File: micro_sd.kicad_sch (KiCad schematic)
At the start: 8 parts, among them IC2 CM1624-08DE, J1 47352-1001, U1 SIP32402ADNP-T1GE4

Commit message: Added footprint for components in Schematics. Updated LED resistors
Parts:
- C33, C34: footprint (none) -> Capacitor_SMD:C_0805_2012Metric
- C35, C36: footprint (none) -> Capacitor_SMD:C_0201_0603Metric
- R8: footprint (none) -> Resistor_SMD:R_0805_2012Metric
- U1: footprint Vishay-T16-0143-04_2016-C-* -> Personal:Vishay-T16-0143-04_2016-C-MFG
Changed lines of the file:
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@@
       (effects (font (size 1.27 1.27)) (justify left))
     )
-    (property "Footprint" "" (id 2) (at 26.67 33.02 0)
+    (property "Footprint" "Capacitor_SMD:C_0805_2012Metric" (id 2) (at 26.67 33.02 0)
       (effects (font (size 1.27 1.27)) hide)
     )
@@
       (effects (font (size 1.27 1.27)) (justify left))
     )
-    (property "Footprint" "" (id 2) (at 172.72 56.515 0)
+    (property "Footprint" "Capacitor_SMD:C_0201_0603Metric" (id 2) (at 172.72 56.515 0)
       (effects (font (size 1.27 1.27)) hide)
     )
@@
       (effects (font (size 1.27 1.27)) (justify left))
     )
-    (property "Footprint" "" (id 2) (at 162.56 56.515 0)
+    (property "Footprint" "Capacitor_SMD:C_0201_0603Metric" (id 2) (at 162.56 56.515 0)
       (effects (font (size 1.27 1.27)) hide)
     )
@@
       (effects (font (size 1.27 1.27)) (justify left))
     )
-    (property "Footprint" "" (id 2) (at 40.64 33.02 0)
+    (property "Footprint" "Resistor_SMD:R_0805_2012Metric" (id 2) (at 40.64 33.02 0)
       (effects (font (size 1.27 1.27)) hide)
     )
@@
       (effects (font (size 1.27 1.27)) (justify left))
     )
-    (property "Footprint" "" (id 2) (at 90.17 30.48 0)
+    (property "Footprint" "Capacitor_SMD:C_0805_2012Metric" (id 2) (at 90.17 30.48 0)
       (effects (font (size 1.27 1.27)) hide)
     )
@@
     (property "Reference" "U1" (id 0) (at 59.69 15.24 0))
     (property "Value" "SIP32402ADNP-T1GE4" (id 1) (at 59.69 17.78 0))
-    (property "Footprint" "Vishay-T16-0143-04_2016-C-*" (id 2) (at 44.45 12.7 0)
-      (effects (font (size 1.27 1.27)) (justify left) hide)
-    )
+    (property "Footprint" "Personal:Vishay-T16-0143-04_2016-C-MFG" (id 2) (at 44.45 12.7 0)
+      (effects (font (size 1.27 1.27)) (justify left) hide)
+    )

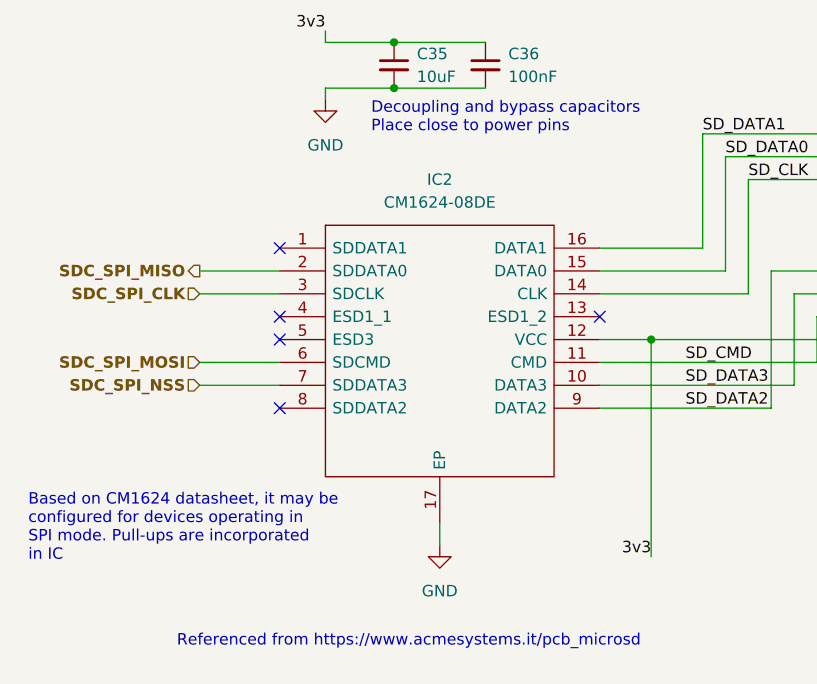
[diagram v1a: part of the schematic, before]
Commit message: Added preliminary PCL layout
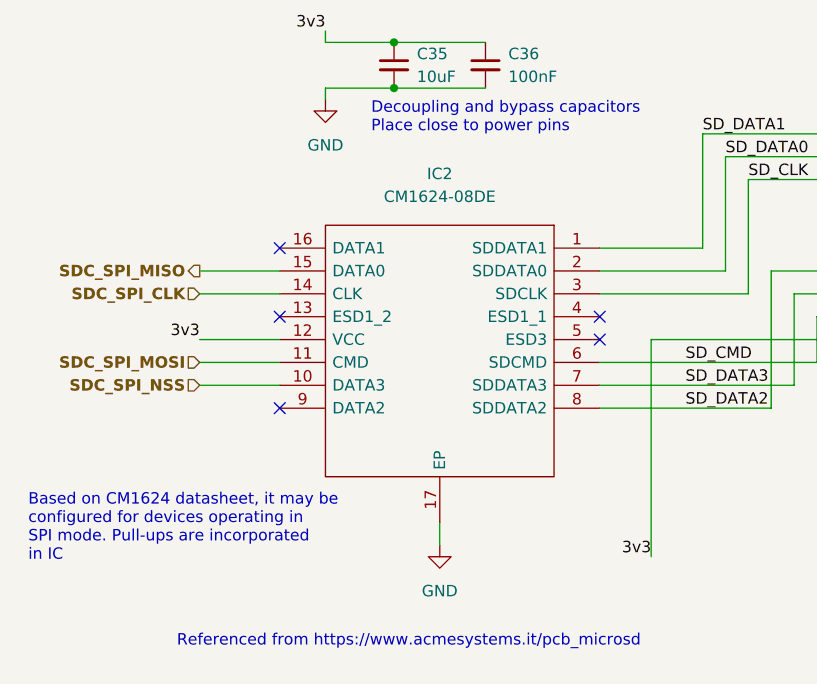
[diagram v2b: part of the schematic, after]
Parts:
- C35, C36: footprint Capacitor_SMD:C_0201_0603Metric -> Capacitor_SMD:C_0603_1608Metric
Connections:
- net SDC_SPI_CLK: now also IC2.14 (CLK); no longer IC2.3 (SDCLK)
- net SDC_SPI_MISO: now also IC2.15 (DATA0); no longer IC2.2 (SDDATA0)
- net SDC_SPI_MOSI: now also IC2.11 (CMD); no longer IC2.6 (SDCMD)
- net SDC_SPI_NSS: now also IC2.10 (DATA3); no longer IC2.7 (SDDATA3)
- net SD_CLK: now also IC2.3 (SDCLK); no longer IC2.14 (CLK)
- net SD_CMD: now also IC2.6 (SDCMD); no longer IC2.11 (CMD)
- net SD_DATA0: now also IC2.2 (SDDATA0); no longer IC2.15 (DATA0)
- net SD_DATA1: now also IC2.1 (SDDATA1); no longer IC2.16 (DATA1)
- net SD_DATA2: now also IC2.8 (SDDATA2); no longer IC2.9 (DATA2)
- net SD_DATA3: now also IC2.7 (SDDATA3); no longer IC2.10 (DATA3)
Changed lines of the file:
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@@
   (junction (at 162.56 59.055) (diameter 0) (color 0 0 0 0)
-  )
-  (junction (at 191.135 86.995) (diameter 0) (color 0 0 0 0)
   )
   (junction (at 40.64 27.94) (diameter 0) (color 0 0 0 0)
@@
   (no_connect (at 149.86 76.835))
   (no_connect (at 149.86 84.455))
-  (no_connect (at 149.86 86.995))
+  (no_connect (at 185.42 86.995))
   (wire (pts (xy 246.38 86.995) (xy 251.46 86.995))
     (stroke (width 0) (type default) (color 0 0 0 0))
@@
     (stroke (width 0) (type default) (color 0 0 0 0))
   )
+  (wire (pts (xy 140.97 86.995) (xy 149.86 86.995))
+    (stroke (width 0) (type default) (color 0 0 0 0))
+  )
   (wire (pts (xy 140.97 81.915) (xy 149.86 81.915))
     (stroke (width 0) (type default) (color 0 0 0 0))
@@
   )
   (wire (pts (xy 72.39 22.86) (xy 90.17 22.86))
-    (stroke (width 0) (type default) (color 0 0 0 0))
-  )
-  (wire (pts (xy 185.42 86.995) (xy 191.135 86.995))
     (stroke (width 0) (type default) (color 0 0 0 0))
   )
@@
     (effects (font (size 1.27 1.27)) (justify left bottom))
   )
+  (label "3v3" (at 140.97 86.995 180)
+    (effects (font (size 1.27 1.27)) (justify right bottom))
+  )
   (label "3v3" (at 191.135 111.125 180)
     (effects (font (size 1.27 1.27)) (justify right bottom))
@@
       (effects (font (size 1.27 1.27)) (justify left))
     )
-    (property "Footprint" "Capacitor_SMD:C_0201_0603Metric" (id 2) (at 172.72 56.515 0)
+    (property "Footprint" "Capacitor_SMD:C_0603_1608Metric" (id 2) (at 172.72 56.515 0)
       (effects (font (size 1.27 1.27)) hide)
     )
@@
       (effects (font (size 1.27 1.27)) (justify left))
     )
-    (property "Footprint" "Capacitor_SMD:C_0201_0603Metric" (id 2) (at 162.56 56.515 0)
+    (property "Footprint" "Capacitor_SMD:C_0603_1608Metric" (id 2) (at 162.56 56.515 0)
       (effects (font (size 1.27 1.27)) hide)
     )
@@
     (pin "8")
   )
-  (symbol (lib_id "SamacSys_Parts:CM1624-08DE") (at 149.86 76.835 0) (unit 1)
-    (in_bom yes) (on_board yes) (fields_autoplaced)
-    (property "Reference" "IC2" (id 0) (at 167.64 69.215 0))
-    (property "Value" "CM1624-08DE" (id 1) (at 167.64 71.755 0))
-    (property "Footprint" "SamacSys_Parts:SON40P135X330X55-17N" (id 2) (at 181.61 74.295 0)
-      (effects (font (size 1.27 1.27)) (justify left) hide)
-    )
-    (property "Datasheet" "http://www.onsemi.com/pub/Collateral/CM1624-D.PDF" (id 3) (at 181.61 76.835 0)
-      (effects (font (size 1.27 1.27)) (justify left) hide)
-    )
-    (property "Description" "ON SEMICONDUCTOR - CM1624-08DE. - EMI Filter, 4-Channel, ESD Protection, 300MHz, Line Protection, UDFN-16" (id 4) (at 181.61 79.375 0)
-      (effects (font (size 1.27 1.27)) (justify left) hide)
-    )
-    (property "Height" "0.55" (id 5) (at 181.61 81.915 0)
-      (effects (font (size 1.27 1.27)) (justify left) hide)
-    )
-    (property "Manufacturer_Name" "onsemi" (id 6) (at 181.61 84.455 0)
-      (effects (font (size 1.27 1.27)) (justify left) hide)
-    )
-    (property "Manufacturer_Part_Number" "CM1624-08DE" (id 7) (at 181.61 86.995 0)
-      (effects (font (size 1.27 1.27)) (justify left) hide)
-    )
-    (property "Mouser Part Number" "748-CM1624-08DE" (id 8) (at 181.61 89.535 0)
-      (effects (font (size 1.27 1.27)) (justify left) hide)
-    )
-    (property "Mouser Price/Stock" "https://www.mouser.co.uk/ProductDetail/onsemi/CM1624-08DE?qs=bXBibfwyPRFMJRiP9A%252BDOw%3D%3D" (id 9) (at 181.61 92.075 0)
-      (effects (font (size 1.27 1.27)) (justify left) hide)
-    )
-    (property "Arrow Part Number" "CM1624-08DE" (id 10) (at 181.61 94.615 0)
-      (effects (font (size 1.27 1.27)) (justify left) hide)
-    )
-    (property "Arrow Price/Stock" "https://www.arrow.com/en/products/cm1624-08de/on-semiconductor?region=nac" (id 11) (at 181.61 97.155 0)
-      (effects (font (size 1.27 1.27)) (justify left) hide)
-    )
-    (property "Mouser Testing Part Number" "" (id 12) (at 181.61 99.695 0)
-      (effects (font (size 1.27 1.27)) (justify left) hide)
-    )
-    (property "Mouser Testing Price/Stock" "" (id 13) (at 181.61 102.235 0)
-      (effects (font (size 1.27 1.27)) (justify left) hide)
-    )
+  (symbol (lib_id "SamacSys_Parts:CM1624-08DE") (at 185.42 76.835 0) (mirror y) (unit 1)
+    (in_bom yes) (on_board yes) (fields_autoplaced)
+    (property "Reference" "IC2" (id 0) (at 167.64 68.58 0))
+    (property "Value" "CM1624-08DE" (id 1) (at 167.64 71.12 0))
+    (property "Footprint" "SamacSys_Parts:SON40P135X330X55-17N" (id 2) (at 153.67 74.295 0)
+      (effects (font (size 1.27 1.27)) (justify left) hide)
+    )
+    (property "Datasheet" "http://www.onsemi.com/pub/Collateral/CM1624-D.PDF" (id 3) (at 153.67 76.835 0)
+      (effects (font (size 1.27 1.27)) (justify left) hide)
+    )
+    (property "Description" "ON SEMICONDUCTOR - CM1624-08DE. - EMI Filter, 4-Channel, ESD Protection, 300MHz, Line Protection, UDFN-16" (id 4) (at 153.67 79.375 0)
+      (effects (font (size 1.27 1.27)) (justify left) hide)
+    )
+    (property "Height" "0.55" (id 5) (at 153.67 81.915 0)
+      (effects (font (size 1.27 1.27)) (justify left) hide)
+    )
+    (property "Manufacturer_Name" "onsemi" (id 6) (at 153.67 84.455 0)
+      (effects (font (size 1.27 1.27)) (justify left) hide)
+    )
+    (property "Manufacturer_Part_Number" "CM1624-08DE" (id 7) (at 153.67 86.995 0)
+      (effects (font (size 1.27 1.27)) (justify left) hide)
+    )
+    (property "Mouser Part Number" "748-CM1624-08DE" (id 8) (at 153.67 89.535 0)
+      (effects (font (size 1.27 1.27)) (justify left) hide)
+    )
+    (property "Mouser Price/Stock" "https://www.mouser.co.uk/ProductDetail/onsemi/CM1624-08DE?qs=bXBibfwyPRFMJRiP9A%252BDOw%3D%3D" (id 9) (at 153.67 92.075 0)
+      (effects (font (size 1.27 1.27)) (justify left) hide)
+    )
+    (property "Arrow Part Number" "CM1624-08DE" (id 10) (at 153.67 94.615 0)
+      (effects (font (size 1.27 1.27)) (justify left) hide)
+    )
+    (property "Arrow Price/Stock" "https://www.arrow.com/en/products/cm1624-08de/on-semiconductor?region=nac" (id 11) (at 153.67 97.155 0)
+      (effects (font (size 1.27 1.27)) (justify left) hide)
+    )
+    (property "Mouser Testing Part Number" "" (id 12) (at 153.67 99.695 0)
+      (effects (font (size 1.27 1.27)) (justify left) hide)
+    )
+    (property "Mouser Testing Price/Stock" "" (id 13) (at 153.67 102.235 0)
+      (effects (font (size 1.27 1.27)) (justify left) hide)
+    )

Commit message: Revision 1 of the board that was manufactured
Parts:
- C33: LCSC (none) -> C1779
- C34: LCSC (none) -> C49678
- C35: LCSC (none) -> C96446
- C36: LCSC (none) -> C14663
- IC2: LCSC (none) -> C605363
- J1: LCSC (none) -> C293569
- R8: LCSC (none) -> C149504
- U1: LCSC (none) -> C143660
